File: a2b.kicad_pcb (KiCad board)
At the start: 2 copper layers, 58.4 x 67.9 mm, 15 parts, among them SW1 SW_DIP_x02, SW2 SW_DIP_x02, SW3 SW_DIP_x02

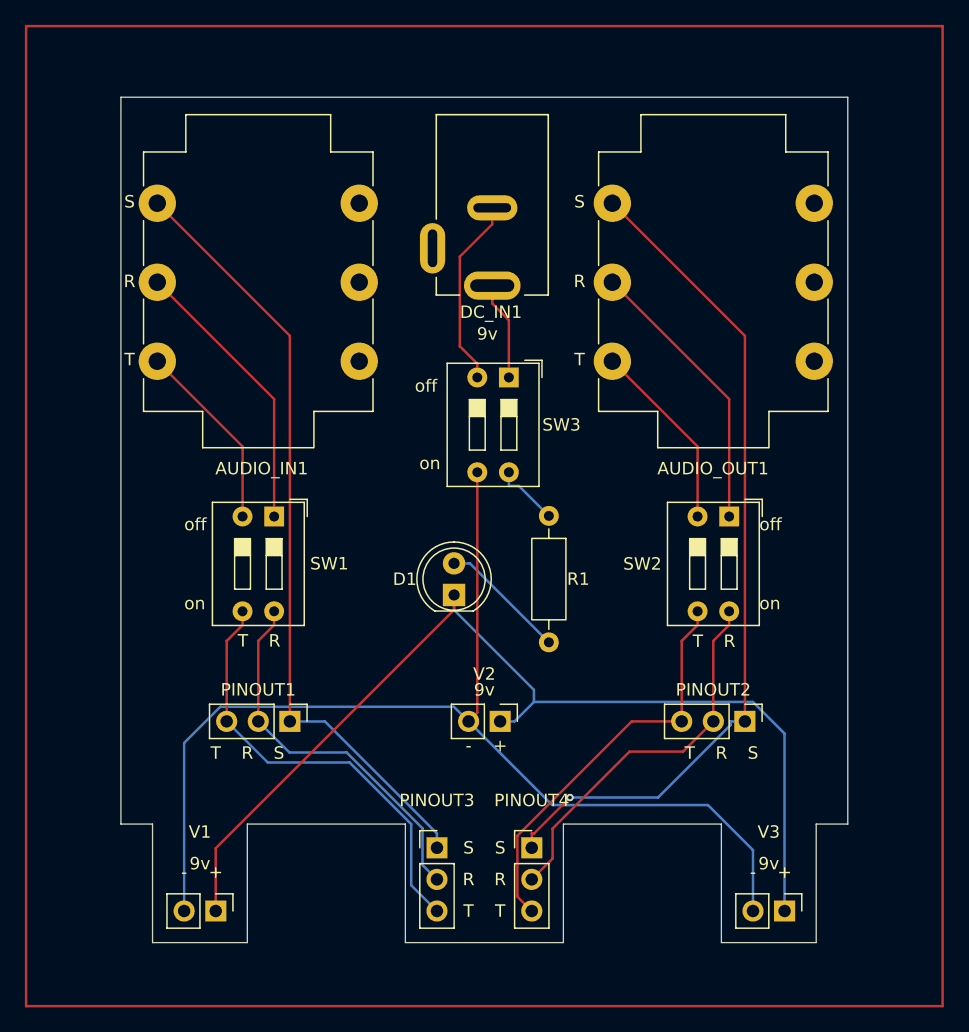
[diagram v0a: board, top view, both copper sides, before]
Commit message: Change 2 switch dip switches from 2 switch to 3 switch so you can control the ground.
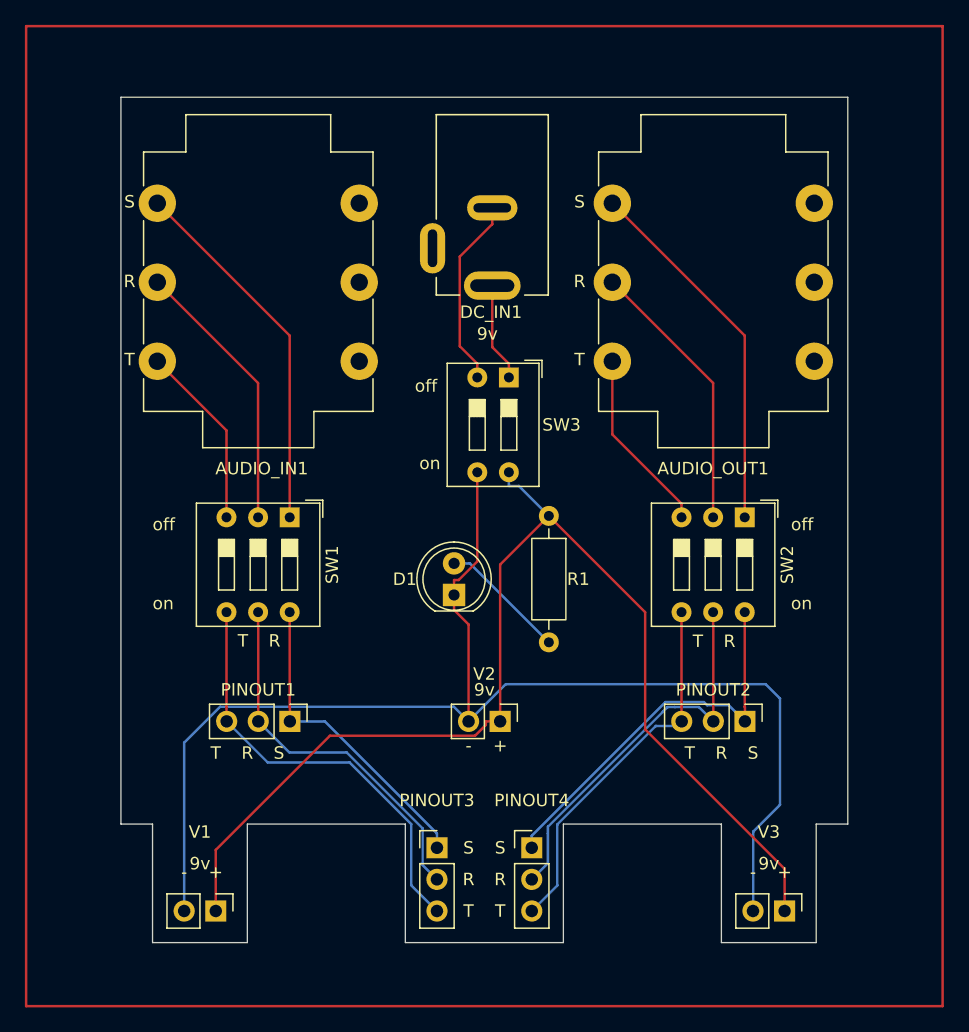
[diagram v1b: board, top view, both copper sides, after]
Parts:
- SW1, SW2: value SW_DIP_x02 -> SW_DIP_x03; footprint Button_Switch_THT:SW_DIP_SPSTx02_Slide_9.78x7.26mm_W7.62mm_P2.54mm -> Button_Switch_THT:SW_DIP_SPSTx03_Slide_9.78x9.8mm_W7.62mm_P2.54mm
- moved SW1 1.25 mm to (132.9, 100.4)
- moved SW2 1.25 mm to (169.5, 100.4)
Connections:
- PINOUT1 pad 1: Net-(AUDIO_IN1-PadS) -> Net-(PINOUT1-Pad1)
- PINOUT2 pad 1: Net-(AUDIO_OUT1-PadS) -> Net-(PINOUT2-Pad1)
- PINOUT3 pad 1: Net-(AUDIO_IN1-PadS) -> Net-(PINOUT1-Pad1)
- PINOUT4 pad 1: Net-(AUDIO_OUT1-PadS) -> Net-(PINOUT2-Pad1)
- SW1 pad 1: Net-(AUDIO_IN1-PadR) -> Net-(AUDIO_IN1-PadS)
- SW1 pad 2: Net-(AUDIO_IN1-PadT) -> Net-(AUDIO_IN1-PadR)
- SW1 pad 3: Net-(PINOUT1-Pad3) -> Net-(AUDIO_IN1-PadT)
- SW1 pad 4: Net-(PINOUT1-Pad2) -> Net-(PINOUT1-Pad3)
- SW2 pad 1: Net-(AUDIO_OUT1-PadR) -> Net-(AUDIO_OUT1-PadS)
- SW2 pad 2: Net-(AUDIO_OUT1-PadT) -> Net-(AUDIO_OUT1-PadR)
- SW2 pad 3: /Net-(PINOUT2-Pad3) -> Net-(AUDIO_OUT1-PadT)
- SW2 pad 4: /Net-(PINOUT2-Pad2) -> /Net-(PINOUT2-Pad3)
- SW3 pad 3: Net-(SW3-Pad3) -> Net-(D1-K)
- V1 pad 1: Net-(D1-K) -> Net-(R1-Pad1)
- V1 pad 2: Net-(SW3-Pad3) -> Net-(D1-K)
- V2 pad 1: Net-(D1-K) -> Net-(R1-Pad1)
- V2 pad 2: Net-(SW3-Pad3) -> Net-(D1-K)
- V3 pad 1: Net-(D1-K) -> Net-(R1-Pad1)
- V3 pad 2: Net-(SW3-Pad3) -> Net-(D1-K)
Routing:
- net Net-(SW3-Pad3): track 90.4 -> 0.00 mm
- net Net-(R1-Pad1): track 5.31 -> 95.3 mm
- net Net-(AUDIO_OUT1-PadS): track 68.2 -> 29.7 mm, vias 1 -> 0
- net Net-(AUDIO_IN1-PadS): track 62.8 -> 29.7 mm
- net Net-(PINOUT2-Pad1): track 0.00 -> 32.0 mm
- net Net-(PINOUT1-Pad1): track 0.00 -> 25.5 mm
- net Net-(D1-K): track 83.4 -> 104.3 mm
- net /Net-(PINOUT2-Pad3): track 32.9 -> 30.0 mm
- net /Net-(PINOUT2-Pad2): track 30.6 -> 31.3 mm
- net Net-(PINOUT1-Pad2): track 30.7 -> 30.1 mm
- net Net-(PINOUT1-Pad3): track 35.5 -> 34.9 mm

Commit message: Swap + & - on board silkscreen and added extra + & - prongs.
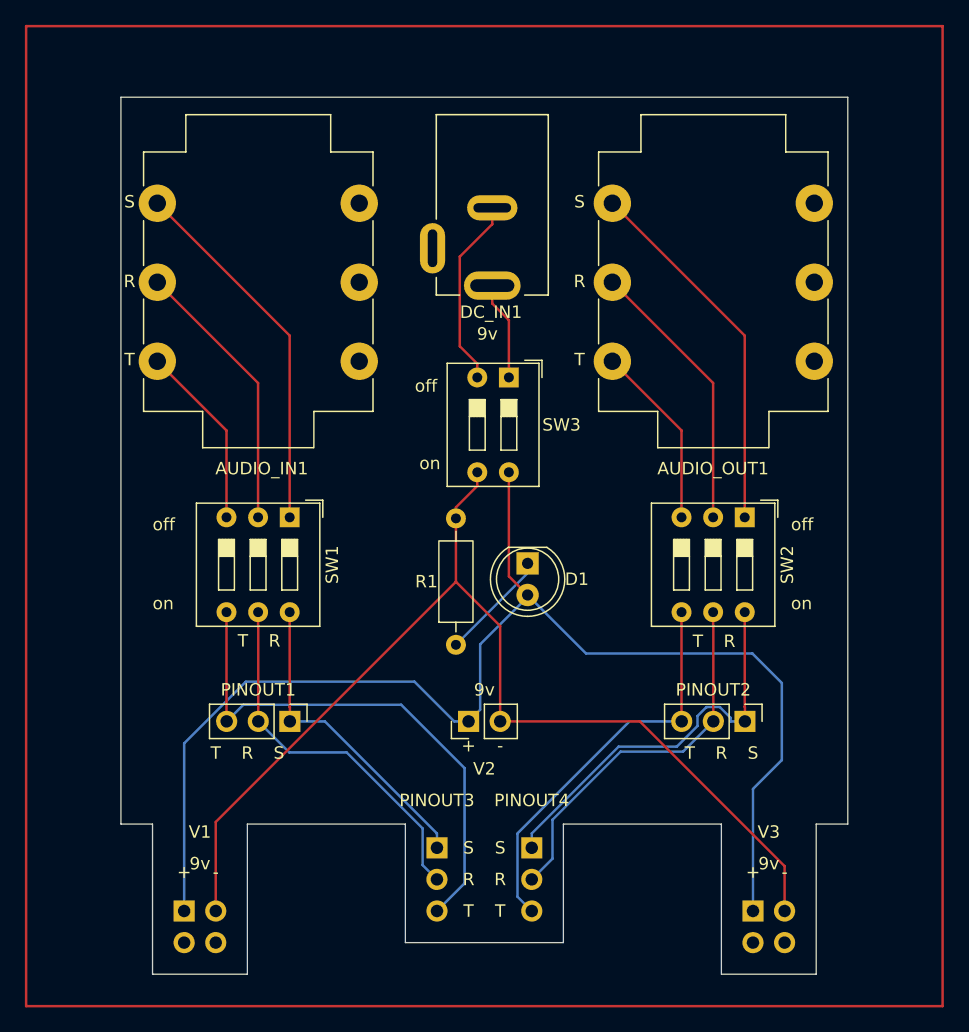
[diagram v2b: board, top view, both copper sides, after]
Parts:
- added REF10: , , F.Cu at (170.2, 134.6)
- added REF12: , , F.Cu at (172.7, 134.6)
- added REF14: , , F.Cu at (124.5, 134.6)
- added REF16: , , F.Cu at (127.0, 134.6)
- moved R1 12.8 mm to (146.3, 110.7), turned to 90 degrees
- moved D1 6.43 mm to (152.1, 104.1), turned to -90 degrees
- moved V2 2.54 mm to (147.3, 116.8), turned to 90 degrees
- moved V1 2.54 mm to (124.5, 132.1), turned to -90 degrees
- moved V3 2.54 mm to (170.2, 132.1), turned to -90 degrees
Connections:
- R1 pad 1: Net-(R1-Pad1) -> Net-(D1-K)
- R1 pad 2: Net-(D1-A) -> Net-(R1-Pad2)
- SW3 pad 3: Net-(D1-K) -> Net-(R1-Pad2)
- SW3 pad 4: Net-(R1-Pad1) -> Net-(D1-A)
- V1 pad 1: Net-(R1-Pad1) -> Net-(D1-A)
- V1 pad 2: Net-(D1-K) -> Net-(R1-Pad2)
- V2 pad 1: Net-(R1-Pad1) -> Net-(D1-A)
- V2 pad 2: Net-(D1-K) -> Net-(R1-Pad2)
- V3 pad 1: Net-(R1-Pad1) -> Net-(D1-A)
- V3 pad 2: Net-(D1-K) -> Net-(R1-Pad2)
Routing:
- net Net-(D1-K): track 104.3 -> 8.93 mm
- net Net-(R1-Pad1): track 95.3 -> 0.00 mm
- net Net-(D1-A): track 10.2 -> 105.0 mm
- net Net-(R1-Pad2): track 0.00 -> 87.9 mm
- net Net-(PINOUT1-Pad3): track 34.9 -> 43.0 mm
- net /Net-(PINOUT2-Pad3): track 30.0 -> 32.4 mm
- net /Net-(PINOUT2-Pad2): track 31.3 -> 30.5 mm
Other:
- board size 58.4 x 67.9 mm -> 58.4 x 70.5 mm

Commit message: update pcb components and routing
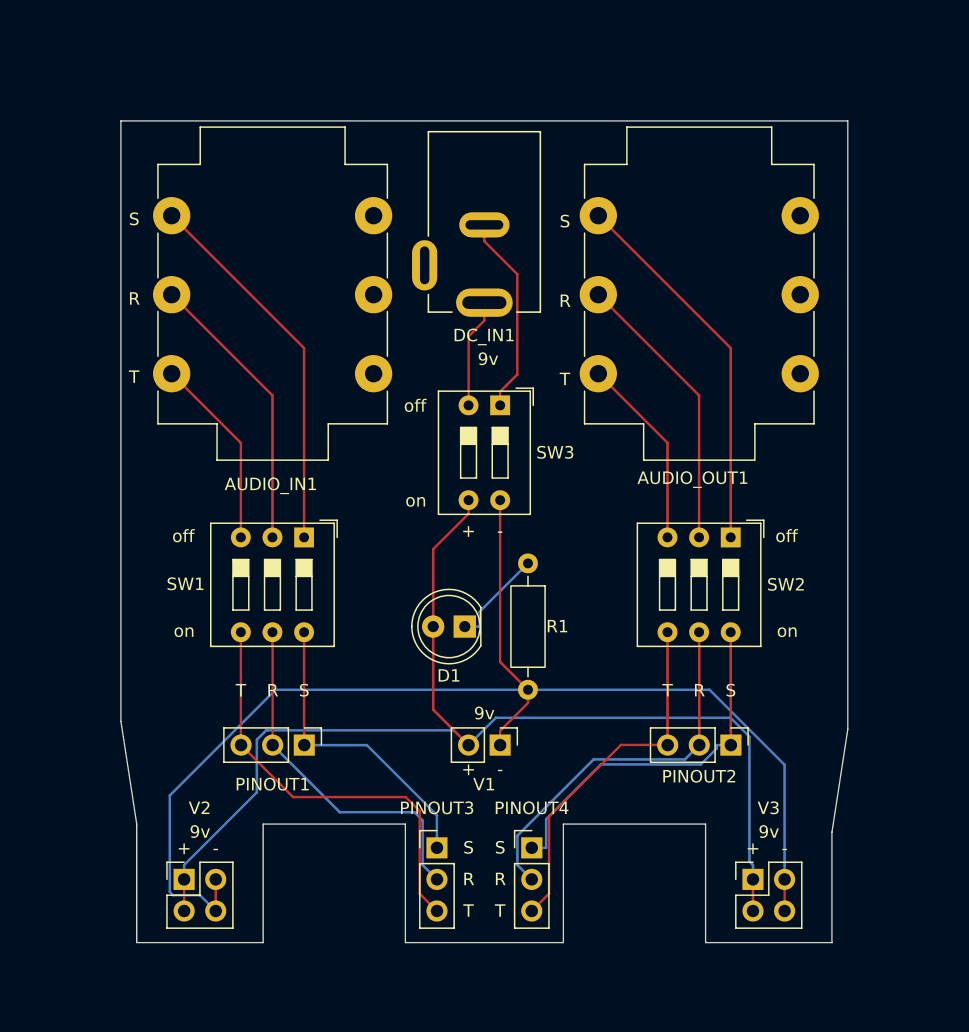
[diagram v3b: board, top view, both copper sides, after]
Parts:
- removed REF10, REF12, REF14, REF16: , 
- PINOUT3, PINOUT4, V1: moved to F.Cu
- V2: footprint Connector_PinHeader_2.54mm:PinHeader_1x02_P2.54mm_Vertical -> Connector_PinHeader_2.54mm:PinHeader_2x02_P2.54mm_Vertical
- V3: footprint Connector_PinHeader_2.54mm:PinHeader_1x02_P2.54mm_Vertical -> Connector_PinHeader_2.54mm:PinHeader_2x02_P2.54mm_Vertical; moved to F.Cu
- moved V1 28.7 mm to (149.9, 118.7)
- moved V2 26.2 mm to (124.5, 129.5), turned to 0 degrees
- moved R1 8.74 mm to (152.1, 104.1), turned to -90 degrees
- moved D1 7.16 mm to (147.0, 109.2), turned to 180 degrees
- moved V3 2.54 mm to (170.2, 129.5), turned to 0 degrees
- moved SW3 2.35 mm to (149.9, 91.4)
- moved PINOUT1 2.23 mm to (134.1, 118.7)
- moved PINOUT2 2.21 mm to (168.4, 118.7)
- moved SW1 1.98 mm to (134.1, 102.1)
- moved SW2 1.97 mm to (168.4, 102.1)
- moved AUDIO_IN1 1.53 mm to (123.5, 88.9)
- moved DC_IN1 1.51 mm to (148.6, 76.9)
- moved AUDIO_OUT1 1.51 mm to (157.7, 88.9)
- turned PINOUT3 to 0 degrees
- turned PINOUT4 to 0 degrees
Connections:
- SW3 pad 1: Net-(DC_IN1-PadPIN) -> Net-(DC_IN1-PadSLEEVE)
- SW3 pad 2: Net-(DC_IN1-PadSLEEVE) -> Net-(DC_IN1-PadPIN)
- SW3 pad 3: Net-(R1-Pad2) -> Net-(D1-A)
- SW3 pad 4: Net-(D1-A) -> Net-(R1-Pad2)
- V1 pad 1: Net-(D1-A) -> Net-(R1-Pad2)
- V1 pad 2: Net-(R1-Pad2) -> Net-(D1-A)
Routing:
- net Net-(R1-Pad2): track 87.9 -> 103.3 mm
- net Net-(D1-A): track 105.0 -> 94.3 mm
- net Net-(PINOUT1-Pad3): track 43.0 -> 34.2 mm
- net /Net-(PINOUT2-Pad3): track 32.4 -> 29.1 mm
- net Net-(PINOUT2-Pad1): track 32.4 -> 30.0 mm
- net Net-(PINOUT1-Pad2): track 30.1 -> 28.9 mm
- net Net-(D1-K): track 8.93 -> 7.89 mm
- net Net-(DC_IN1-PadSLEEVE): track 15.3 -> 16.2 mm
- net Net-(DC_IN1-PadPIN): track 7.93 -> 8.78 mm
- net Net-(PINOUT1-Pad1): track 25.5 -> 24.7 mm
- net Net-(AUDIO_OUT1-PadT): track 14.8 -> 15.5 mm
- net Net-(AUDIO_OUT1-PadS): track 29.7 -> 30.3 mm
- net Net-(AUDIO_OUT1-PadR): track 22.3 -> 22.9 mm
- net Net-(AUDIO_IN1-PadS): track 29.7 -> 30.3 mm
- net Net-(AUDIO_IN1-PadR): track 22.3 -> 22.9 mm
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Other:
- board size 58.4 x 70.5 mm -> 58.4 x 66 mm
